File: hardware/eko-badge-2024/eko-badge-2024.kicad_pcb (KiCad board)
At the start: 2 copper layers, 47.5 x 108.1 mm, 56 parts, among them J1 UART, J2 Battery, J3 Lentes, J4 OLED, J5 Add-On, J6 Add-On, J7 Battery, P1 USB_C_Plug_USB2.0, Q1 DMG3415U-7, SW1 ON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

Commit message: feat(Hw):Added_details
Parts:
- F1: value 0.75A -> 1A
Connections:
- J3 pad 1: unconnected-(J3-Pin_1-Pad1) -> /VOUT
- J3 pad 2: unconnected-(J3-Pin_2-Pad2) -> GND
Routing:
- net GND: track 189.0 -> 212.5 mm, vias 27 -> 30
- net /VOUT: track 215.1 -> 224.1 mm, vias 9 -> 10

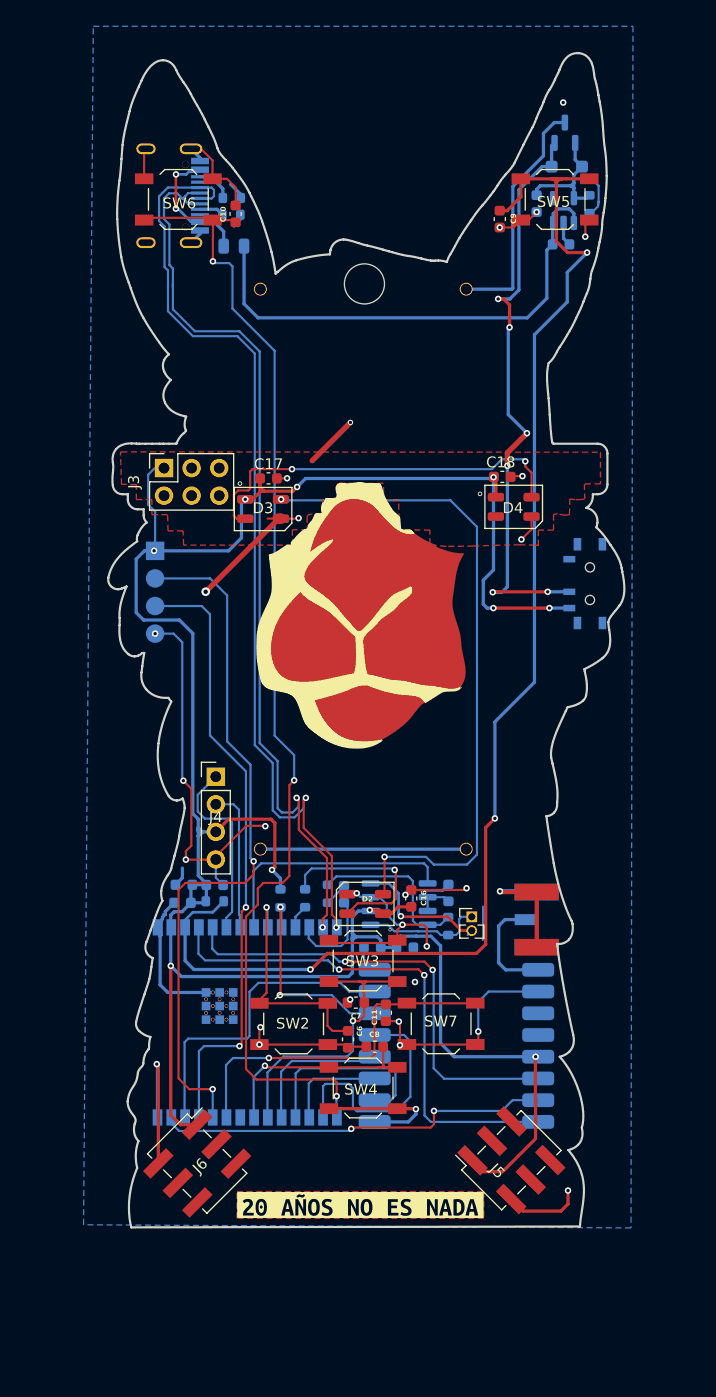
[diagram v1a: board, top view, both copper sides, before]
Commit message: feat(Hw):Added_Speaker_Holes
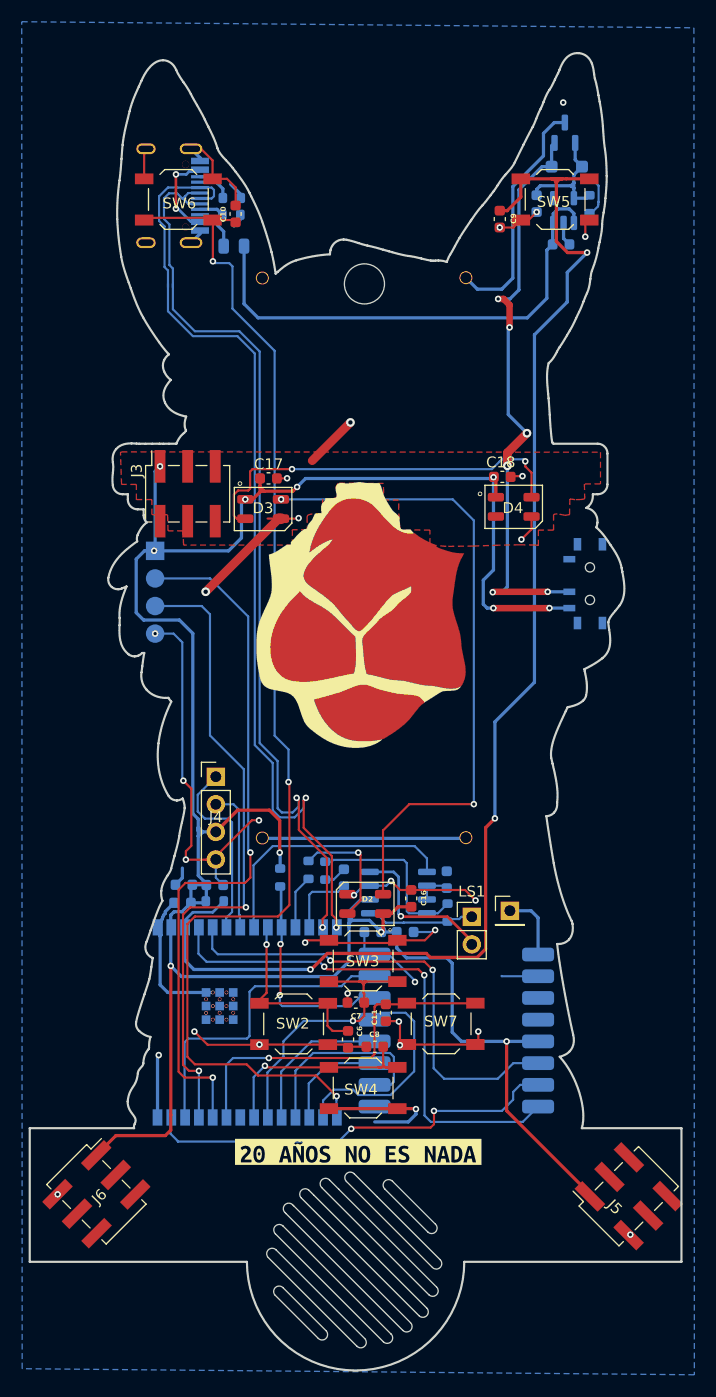
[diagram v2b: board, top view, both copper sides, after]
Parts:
- removed the Ref** at (203.7, 84.0)
- AE1: footprint Eko2024:SMA_EDGE -> Connector_PinHeader_2.54mm:PinHeader_1x01_P2.54mm_Vertical; moved to F.Cu
- J3: footprint Connector_PinSocket_2.54mm:PinSocket_2x03_P2.54mm_Vertical -> Connector_PinSocket_2.54mm:PinSocket_2x03_P2.54mm_Vertical_SMD
- LS1: footprint Connector_PinHeader_1.27mm:PinHeader_1x02_P1.27mm_Vertical -> Connector_PinHeader_2.54mm:PinHeader_1x02_P2.54mm_Vertical
- U3: value RFM95W-868S2 -> RFM95W-915S2
- moved J5 11.3 mm to (227.8, 135.4)
- moved J6 9.70 mm to (178.7, 135.2)
- moved kibuzzard-66BD383E 4.89 mm to (202.8, 131.3)
- moved AE1 4.58 mm to (216.8, 109.1), turned to 0 degrees
- moved J3 3.21 mm to (187.1, 70.7)
- moved R7 2.63 mm to (198.3, 105.3)
- moved R5 2.14 mm to (199.8, 105.4)
- moved R8 1.92 mm to (195.7, 106.0)
- moved C13 1.52 mm to (201.5, 106.0)
- moved C12 1.43 mm to (204.2, 111.0)
- moved C15 1.43 mm to (207.2, 111.0)
- moved U3 1.41 mm to (211.9, 120.1)
- moved R6 1.24 mm to (211.1, 109.2)
- moved C14 1.23 mm to (211.0, 106.2)
- moved U4 1.06 mm to (206.6, 107.4)
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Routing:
- net GND: track 212.5 -> 187.4 mm
- net /BOOT: track 105.7 -> 115.0 mm
- net Net-(D2-DIN): track 17.6 -> 11.1 mm
- net /VOUT: track 224.1 -> 228.6 mm, vias 10 -> 11
- net Net-(AE1-A): track 10.0 -> 6.25 mm
- net /LEFT: track 21.5 -> 17.8 mm
- net /TX: track 56.8 -> 59.6 mm
- net /PIN: track 2.22 -> 4.96 mm
- net /DIO1: track 36.2 -> 38.6 mm
- net Net-(D2-DOUT): track 62.0 -> 59.9 mm
- net /CS: track 22.3 -> 20.3 mm
- net /IO11: track 8.29 -> 6.52 mm
- net Net-(U4-VO-): track 12.8 -> 14.3 mm
- net Net-(U4-VO+): track 11.1 -> 9.96 mm
- net /SD: track 23.5 -> 24.5 mm
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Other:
- board size 47.5 x 108.1 mm -> 60 x 121.3 mm

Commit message: feat(hw): add logo pcbway and EC
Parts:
- added G***: LOGO, Aesthetics:electronic_cats_logo_8x6, B.Cu at (190.8, 132.6)
- added G***: LOGO, LOGO, B.Cu at (222.1, 137.1)
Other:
- board text added: "#laeko"
- board text added: "#latam"
- board text added: "#vamosalasado"
- board text added: "#volviolabarra"
- board text added: "Con amor desde México"
- board text added: "Sponsored by"
- board text added: "We Parce Serote Che"

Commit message: feat: update labels
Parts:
- added kibuzzard-66D79F47: G***, kibuzzard-66D79F47, B.Cu at (179.3, 138.5)
- added kibuzzard-66D79F5F: G***, kibuzzard-66D79F5F, B.Cu at (179.1, 140.3)
- added kibuzzard-66D79F90: G***, kibuzzard-66D79F90, B.Cu at (189.7, 137.5)
- added kibuzzard-66D79FA5: G***, kibuzzard-66D79FA5, B.Cu at (189.6, 139.9)
- added kibuzzard-66D7A032: G***, kibuzzard-66D7A032, B.Cu at (179.9, 131.1)
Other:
- board text added: "Parce Serote Che"
- board text removed: "#laeko"
- board text removed: "#latam"
- board text removed: "#vamosalasado"
- board text removed: "#volviolabarra"
- board text removed: "Con amor desde México"
- board text removed: "We Parce Serote Che"

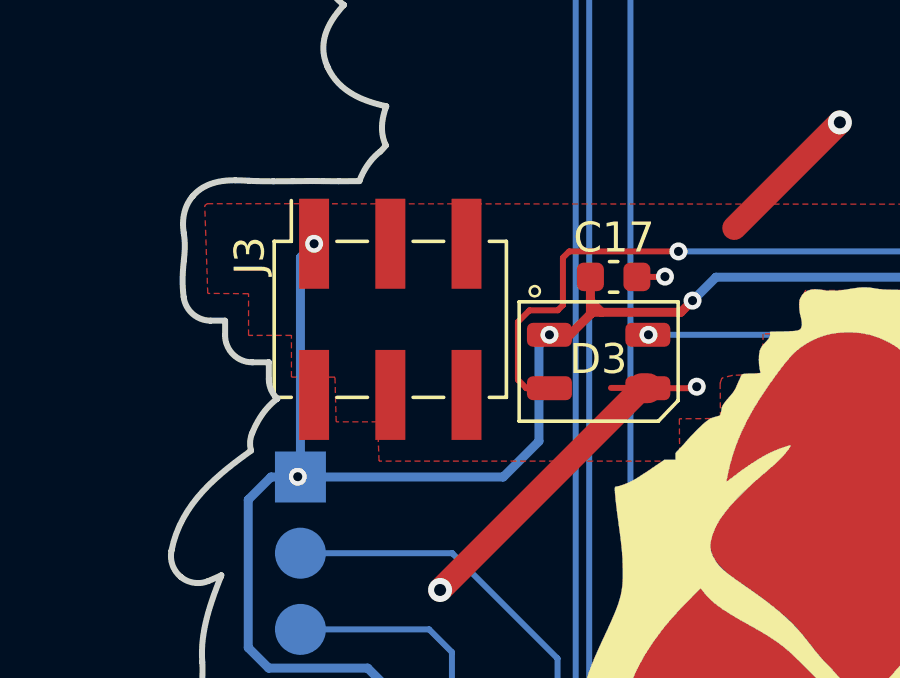
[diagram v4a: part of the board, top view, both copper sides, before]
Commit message: feat(Hw):Update_Connector_Pinsocket
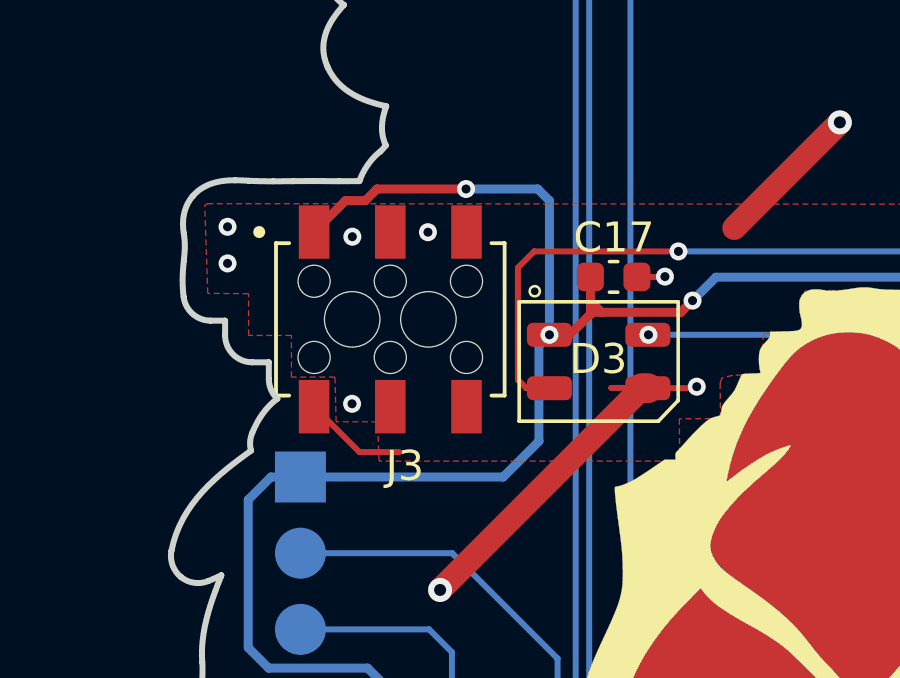
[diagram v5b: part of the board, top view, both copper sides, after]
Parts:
- J3: footprint Connector_PinSocket_2.54mm:PinSocket_2x03_P2.54mm_Vertical_SMD -> Eko2024:HARWIN_M20-7810345
- turned J3 to 180 degrees
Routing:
- net /VOUT: track 228.6 -> 233.5 mm, vias 11 -> 10
- net GND: track 187.4 -> 190.8 mm, vias 30 -> 35

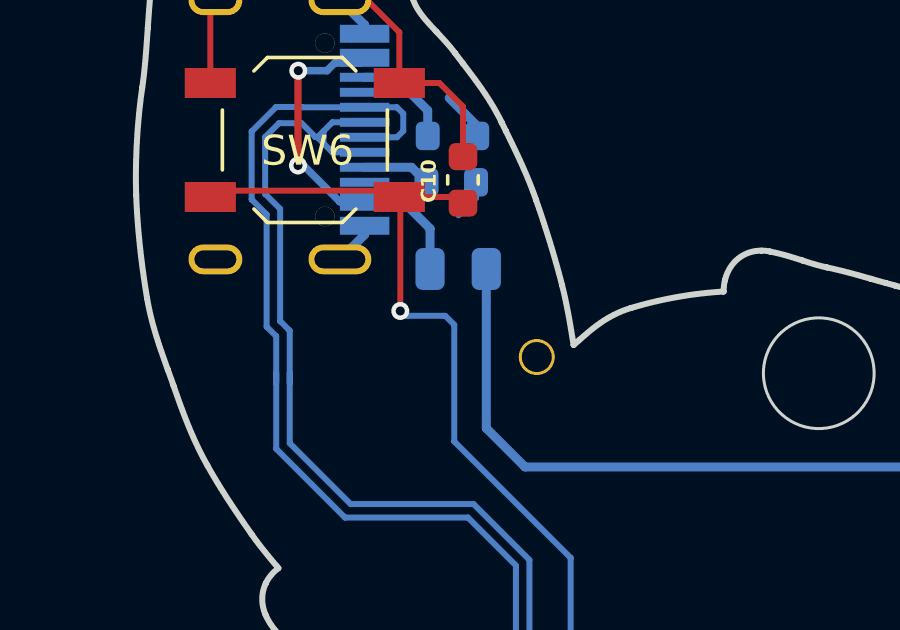
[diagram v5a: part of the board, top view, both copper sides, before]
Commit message: feat(Hw):Update_BoM
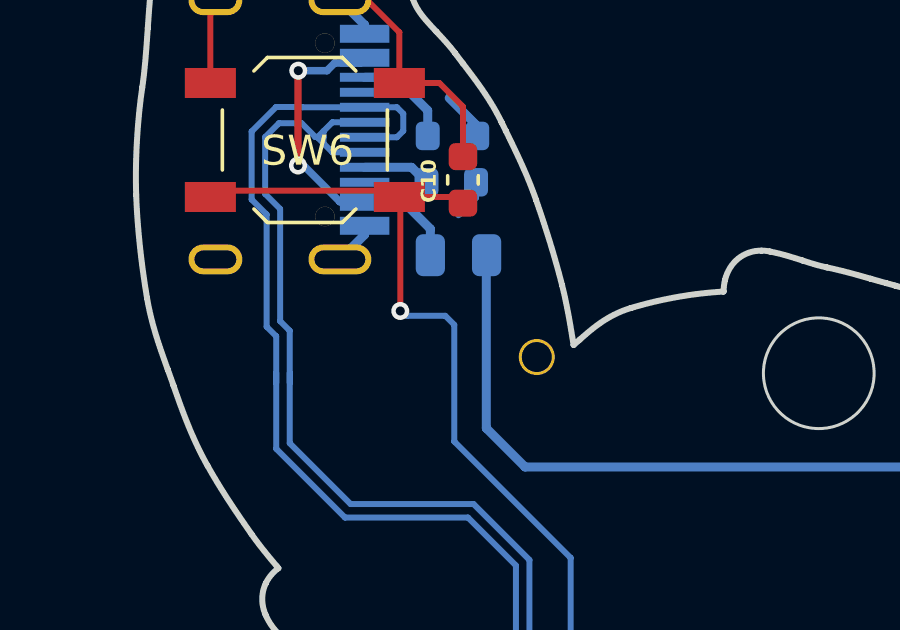
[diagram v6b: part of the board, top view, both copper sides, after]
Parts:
- added kibuzzard-66E4B147: G***, kibuzzard-66E4B147, B.Cu at (222.3, 86.0)
- moved F1 0.46 mm to (191.4, 47.4)
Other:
- board text added: "v1.1"
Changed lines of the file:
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@@
 		(at 187.145 70.695 180)
 		(property "Reference" "J3"
-			(at -0.485 -4.885 360)
+			(at -0.485 -4.885 0)
 			(layer "F.SilkS")
 			(effects
@@
 		)
 		(property "Value" "Lentes"
-			(at 7.77 4.865 360)
+			(at 7.77 4.865 0)
 			(layer "F.Fab")
 			(effects
@@
 		)
 		(property "Footprint" "Eko2024:HARWIN_M20-7810345"
-			(at 0 0 360)
+			(at 0 0 0)
 			(layer "F.Fab")
 			(hide yes)
@@
 		)
 		(property "Datasheet" ""
-			(at 0 0 360)
+			(at 0 0 0)
 			(layer "F.Fab")
 			(hide yes)
@@
 		)
 		(property "Description" ""
-			(at 0 0 360)
+			(at 0 0 0)
 			(layer "F.Fab")
 			(hide yes)
@@
 		)
 	)
+	(footprint "kibuzzard-66E4B147"
+		(layer "B.Cu")
+		(at 222.31 85.95 -90)
+		(descr "Generated with KiBuzzard")
+		(tags "kb_params=eyJBbGlnbm1lbnRDaG9pY2UiOiAiQ2VudGVyIiwgIkNhcExlZnRDaG9pY2UiOiAiWyIsICJDYXBSaWdodENob2ljZSI6ICJdIiwgIkZvbnRDb21ib0JveCI6ICJGcmVkZHlTcGFyay1SZWd1bGFyIiwgIkhlaWdodEN0cmwiOiAxLjUsICJMYXllckNvbWJvQm94IjogIkYuU2lsa1MiLCAiTGluZVNwYWNpbmdDdHJsIjogMS4wLCAiTXVsdGlMaW5lVGV4dCI6ICJPTiIsICJQYWRkaW5nQm90dG9tQ3RybCI6IDEuMCwgIlBhZGRpbmdMZWZ0Q3RybCI6IDEuMCwgIlBhZGRpbmdSaWdodEN0cmwiOiAxLjAsICJQYWRkaW5nVG9wQ3RybCI6IDEuMCwgIldpZHRoQ3RybCI6IDEuNSwgImFkdmFuY2VkQ2hlY2tib3giOiBmYWxzZSwgImlubGluZUZvcm1hdFRleHRib3giOiBmYWxzZSwgImxpbmVvdmVyU3R5bGVDaG9pY2UiOiAiU3F1YXJlIiwgImxpbmVvdmVyVGhpY2tuZXNzQ3RybCI6IDF9")
+		(property "Reference" "kibuzzard-66E4B147"
+			(at 0 3.998286 90)
+			(layer "B.SilkS")
+			(hide yes)
+			(effects
+				(font
+					(size 0.001 0.001)
+				)
+				(justify mirror)
+			)
+		)
+		(property "Value" "G***"
+			(at 0 -3.998286 90)
+			(layer "B.SilkS")
+			(hide yes)
+			(effects
+				(font
+					(size 0.001 0.001)
+				)
+				(justify mirror)
+			)
+		)
+		(property "Footprint" ""
+			(at 0 0 90)
+			(layer "B.Fab")
+			(hide yes)
+			(effects
+				(font
+					(size 1.27 1.27)
+					(thickness 0.15)
+				)
+				(justify mirror)
+			)
+		)
+		(property "Datasheet" ""
+			(at 0 0 90)
+			(layer "B.Fab")
+			(hide yes)
+			(effects
+				(font
+					(size 1.27 1.27)
+					(thickness 0.15)
+				)
+				(justify mirror)
+			)
+		)
+		(property "Description" ""
+			(at 0 0 90)
+			(layer "B.Fab")
+			(hide yes)
+			(effects
+				(font
+					(size 1.27 1.27)
+					(thickness 0.15)
+				)
+				(justify mirror)
+			)
+		)
+		(attr board_only exclude_from_pos_files exclude_from_bom)
+		(fp_poly
+			(pts
+				(xy -0.704936 -0.378755) (xy -0.568401 -0.351663) (xy -0.454936 -0.270386) (xy -0.378487 -0.148873)
+				(xy -0.353004 -0.001073) (xy -0.378755 0.145655) (xy -0.456009 0.26824) (xy -0.569206 0.351127)
+				(xy -0.70279 0.378755) (xy -0.837983 0.351127) (xy -0.951717 0.26824) (xy -1.02897 0.145655) (xy -1.054721 -0.001073)
+				(xy -1.028702 -0.14485) (xy -0.950644 -0.267167) (xy -0.837178 -0.350858) (xy -0.704936 -0.378755)
+			)
+			(stroke
+				(width 0)
+				(type solid)
+			)
+			(fill solid)
+			(layer "B.SilkS")
+		)
+		(fp_poly
+			(pts
+				(xy -1.447425 0.950286) (xy -1.626252 0.950286) (xy -1.626252 -0.950286) (xy -1.447425 -0.950286)
+				(xy -0.694206 -0.950286) (xy -0.694206 -0.771459) (xy -0.844152 -0.757511) (xy -0.982833 -0.715665)
+				(xy -1.110247 -0.645923) (xy -1.226395 -0.548283) (xy -1.323095 -0.430928) (xy -1.392167 -0.302039)
+				(xy -1.433611 -0.161615) (xy -1.447425 -0.009657) (xy -1.434013 0.147264) (xy -1.393777 0.291845)
+				(xy -1.326717 0.424088) (xy -1.232833 0.543991) (xy -1.119769 0.643509) (xy -0.995172 0.714592)
+				(xy -0.85904 0.757242) (xy -0.711373 0.771459) (xy -0.560622 0.757444) (xy -0.421674 0.715397) (xy -0.294528 0.645319)
+				(xy -0.179185 0.54721) (xy -0.083423 0.428849) (xy -0.015021 0.298015) (xy 0.026019 0.154708) (xy 0.0397 -0.001073)
+				(xy 0.02622 -0.154171) (xy -0.014217 -0.295869) (xy -0.081612 -0.426167) (xy -0.175966 -0.545064)
+				(xy -0.28923 -0.644112) (xy -0.413358 -0.714861) (xy -0.54835 -0.75731) (xy -0.694206 -0.771459)
+				(xy -0.694206 -0.950286) (xy 0.322961 -0.950286) (xy 0.322961 -0.747854) (xy 0.212446 -0.732833)
+				(xy 0.154506 -0.684549) (xy 0.13412 -0.625536) (xy 0.129828 -0.550429) (xy 0.129828 0.563305) (xy 0.13412 0.635193)
+				(xy 0.155579 0.69206) (xy 0.214592 0.738197) (xy 0.327253 0.752146) (xy 0.424893 0.73927) (xy 0.479614 0.712446)
+				(xy 0.51824 0.668455) (xy 1.054721 -0.052575) (xy 1.054721 0.563305) (xy 1.059013 0.63412) (xy 1.080472 0.690987)
+				(xy 1.140558 0.737124) (xy 1.252146 0.752146) (xy 1.363734 0.737124) (xy 1.42382 0.687768) (xy 1.444206 0.628755)
+				(xy 1.447425 0.554721) (xy 1.447425 -0.552575) (xy 1.444206 -0.626609) (xy 1.42382 -0.684549) (xy 1.363734 -0.732833)
+				(xy 1.25 -0.747854) (xy 1.139485 -0.736052) (xy 1.07618 -0.689914) (xy 0.520386 0.043991) (xy 0.520386 -0.552575)
+				(xy 0.517167 -0.626609) (xy 0.496781 -0.684549) (xy 0.436695 -0.732833) (xy 0.322961 -0.747854)
+				(xy 0.322961 -0.950286) (xy 1.447425 -0.950286) (xy 1.626252 -0.950286) (xy 1.626252 0.950286) (xy 1.447425 0.950286)
+				(xy -1.447425 0.950286)
+			)
+			(stroke
+				(width 0)
+				(type solid)
+			)
+			(fill solid)
+			(layer "B.SilkS")
+		)
+	)
 	(footprint "Resistor_SMD:R_0603_1608Metric"
 		(layer "B.Cu")
@@
 		(tags "resistor")
 		(property "Reference" "R3"
-			(at -1.43 -1.33 0)
+			(at -1.96 -0.85 0)
 			(layer "B.SilkS")
 			(effects
@@
 	(footprint "Fuse:Fuse_0805_2012Metric"
 		(layer "B.Cu")
-		(at 191.4 47.9)
+		(at 191.41 47.44)
 		(descr "Fuse SMD 0805 (2012 Metric), square (rectangular) end terminal, IPC_7351 nominal, (Body size source: https://docs.google.com/spreadsheets/d/1BsfQQcO9C6DZCsRaXUlFlo91Tg2WpOkGARC1WS5S8t0/edit?usp=sharing), generated with kicad-footprint-generator")
 		(tags "fuse")
@@
 		)
 	)
+	(gr_text "v1.1"
+		(at 209.65 51.05 0)
+		(layer "B.SilkS")
+		(effects
+			(font
+				(size 1 1)
+				(thickness 0.1)
+			)
+			(justify left bottom mirror)
+		)
+	)
 	(gr_text "Sponsored by"
 		(at 228.53 132.22 0)
@@
 	)
 	(segment
-		(start 192.3375 53.2075)
-		(end 193.63 54.5)
+		(start 220.8 45.76)
+		(end 220.8 44.92)
 		(width 0.3)
 		(layer "B.Cu")
@@
 	)
 	(segment
-		(start 220.8 45.76)
-		(end 220.8 44.92)
+		(start 218.41 54.5)
+		(end 220.21 52.7)
 		(width 0.3)
 		(layer "B.Cu")
@@
 	)
 	(segment
-		(start 222.7 44.89)
-		(end 222.7 45.76)
+		(start 193.63 54.5)
+		(end 218.41 54.5)
 		(width 0.3)
 		(layer "B.Cu")
@@
 	)
 	(segment
-		(start 220.21 48.27)
-		(end 220.745 47.735)
+		(start 192.3475 47.44)
+		(end 192.3375 47.45)
+		(width 0.3)
+		(layer "B.Cu")
+		(net 3)
+	)
+	(segment
+		(start 222.7 44.89)
+		(end 222.7 45.76)
 		(width 0.3)
 		(layer "B.Cu")
@@
 	)
 	(segment
-		(start 218.41 54.5)
-		(end 220.21 52.7)
+		(start 192.3375 47.45)
+		(end 192.3375 53.2075)
 		(width 0.3)
 		(layer "B.Cu")
@@
 	)
 	(segment
-		(start 222.28 44.47)
-		(end 222.7 44.89)
+		(start 192.3375 53.2075)
+		(end 193.63 54.5)
 		(width 0.3)
 		(layer "B.Cu")
@@
 	)
 	(segment
-		(start 192.3375 47.9)
-		(end 192.3375 53.2075)
+		(start 220.21 48.27)
+		(end 220.745 47.735)
 		(width 0.3)
 		(layer "B.Cu")
@@
 	)
 	(segment
-		(start 193.63 54.5)
-		(end 218.41 54.5)
+		(start 222.28 44.47)
+		(end 222.7 44.89)
 		(width 0.3)
 		(layer "B.Cu")
@@
 	)
 	(segment
-		(start 188.2825 45.66)
-		(end 189.57 45.66)
-		(width 0.3)
-		(layer "B.Cu")
-		(net 17)
-	)
-	(segment
 		(start 186.07 41.29)
 		(end 187.027449 41.29)
@@
 	)
 	(segment
-		(start 189.57 45.66)
-		(end 190.4625 46.5525)
+		(start 188.2825 45.66)
+		(end 189.57 45.66)
 		(width 0.3)
 		(layer "B.Cu")
@@
 	)
 	(segment
-		(start 190.4625 46.5525)
-		(end 190.4625 47.9)
+		(start 189.57 45.66)
+		(end 190.4725 46.5625)
+		(width 0.3)
+		(layer "B.Cu")
+		(net 17)
+	)
+	(segment
+		(start 190.4725 46.5625)
+		(end 190.4725 47.44)
 		(width 0.3)
 		(layer "B.Cu")
